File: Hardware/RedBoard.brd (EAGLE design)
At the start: 68.6 x 54.4 mm, 65 parts, among them IC3 LM1117, J1 POWER_JACKOVERPASTE_REDBOARD_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, J2 ICSP, Q1 ZXMP6A13FTA, Q2 2N7002PW, U1 FT231XS, U2 MIC5205, U3 ATMEGA328, Y1 16MHz

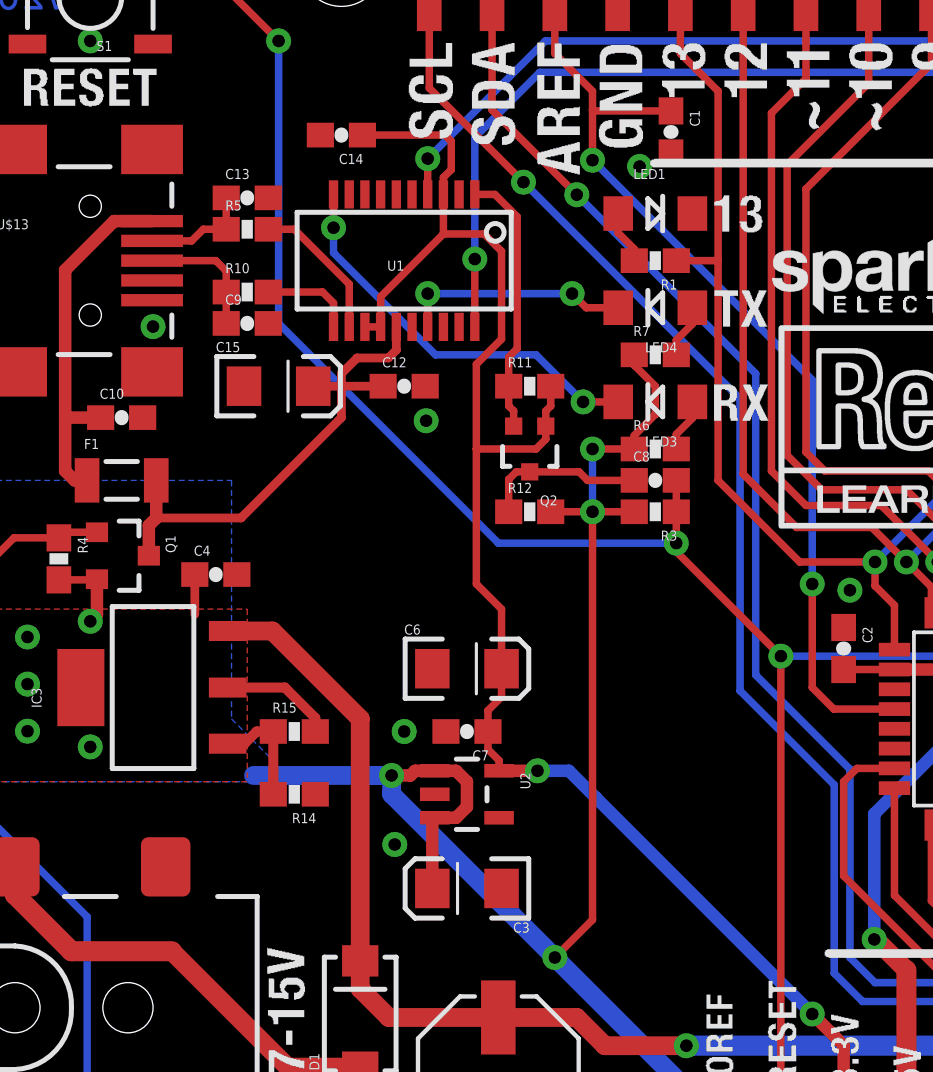
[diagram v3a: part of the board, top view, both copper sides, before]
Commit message: Spacing out caps and resistors
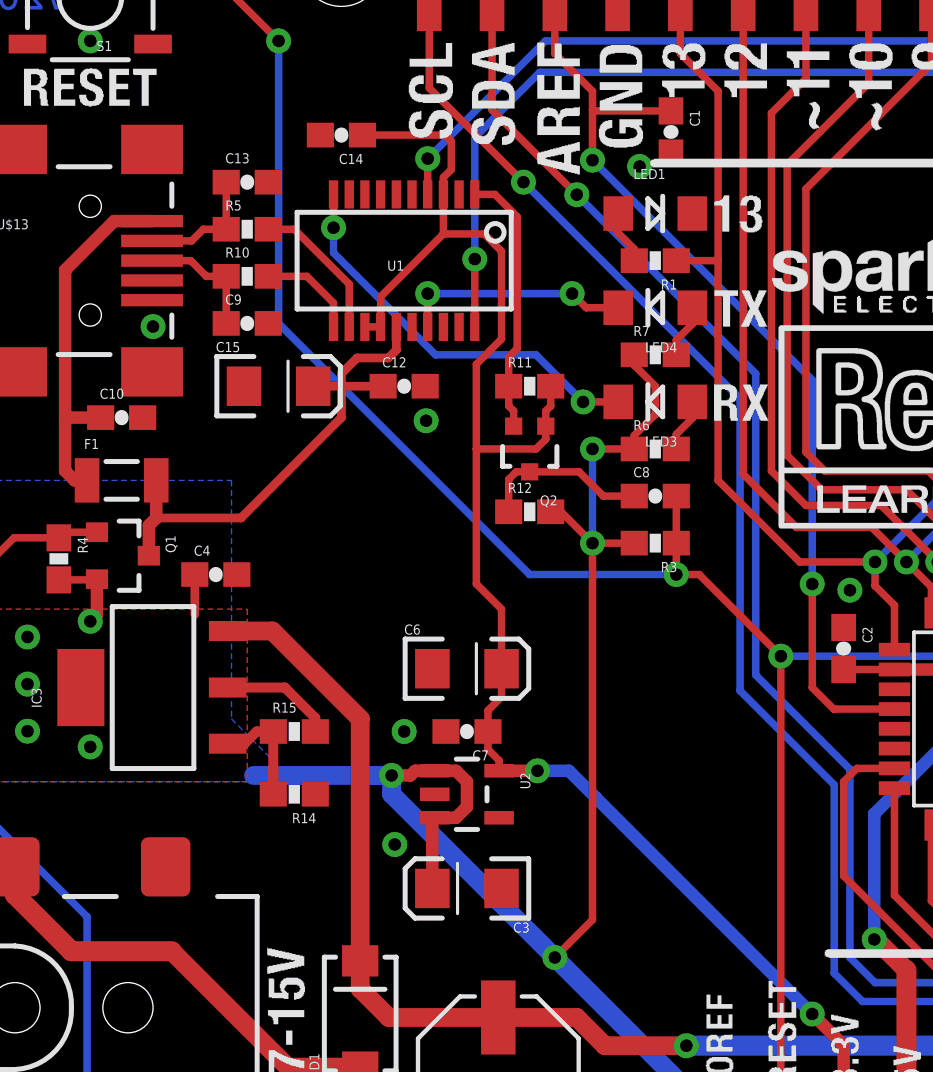
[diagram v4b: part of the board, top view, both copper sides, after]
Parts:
- moved R3 1.27 mm to (27.9, 27.9)
- moved C13 0.64 mm to (11.4, 42.5)
- moved C8 0.64 mm to (27.9, 29.8)
- moved R10 0.63 mm to (11.4, 38.7)
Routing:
- net D-: track 4.46 -> 5.10 mm
- net 5V: track 165.1 -> 165.7 mm
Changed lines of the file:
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@@
 <layer number="20" name="Dimension" color="15" fill="1" visible="yes" active="yes"/>
 <layer number="21" name="tPlace" color="16" fill="1" visible="yes" active="yes"/>
-<layer number="22" name="bPlace" color="14" fill="1" visible="no" active="yes"/>
+<layer number="22" name="bPlace" color="14" fill="1" visible="yes" active="yes"/>
 <layer number="23" name="tOrigins" color="15" fill="1" visible="yes" active="yes"/>
 <layer number="24" name="bOrigins" color="15" fill="1" visible="yes" active="yes"/>
@@
 <layer number="47" name="Measures" color="7" fill="1" visible="no" active="yes"/>
 <layer number="48" name="Document" color="7" fill="1" visible="no" active="yes"/>
-<layer number="49" name="ReferenceLC" color="13" fill="1" visible="yes" active="yes"/>
+<layer number="49" name="ReferenceLC" color="13" fill="1" visible="no" active="yes"/>
 <layer number="50" name="ReferenceLS" color="12" fill="1" visible="no" active="yes"/>
 <layer number="51" name="tDocu" color="6" fill="1" visible="yes" active="yes"/>
@@
 </element>
 <element name="R2" library="SparkFun" package="0603-RES" value="1k" x="58.42" y="34.29"/>
-<element name="R3" library="SparkFun" package="0603-RES" value="10k" x="27.94" y="29.21" smashed="yes" rot="R180">
-<attribute name="NAME" x="28.829" y="28.448" size="0.4064" layer="25" font="vector" rot="R180"/>
-<attribute name="VALUE" x="29.464" y="29.083" size="0.4064" layer="27" font="vector"/>
+<element name="R3" library="SparkFun" package="0603-RES" value="10k" x="27.94" y="27.94" smashed="yes" rot="R180">
+<attribute name="NAME" x="28.829" y="27.178" size="0.4064" layer="25" font="vector" rot="R180"/>
+<attribute name="VALUE" x="29.464" y="27.813" size="0.4064" layer="27" font="vector"/>
 </element>
 <element name="S1" library="SparkFun" package="TACTILE_SWITCH_SMD" value="RESET" x="5.08" y="50.038" rot="R180"/>
@@
 <attribute name="VALUE" x="4.826" y="28.829" size="0.4064" layer="27"/>
 </element>
-<element name="C8" library="SparkFun" package="0603-CAP" value="0.1uF" x="27.94" y="30.48" smashed="yes">
-<attribute name="NAME" x="27.051" y="31.242" size="0.4064" layer="25" font="vector"/>
-<attribute name="VALUE" x="29.464" y="30.226" size="0.4064" layer="27" font="vector"/>
+<element name="C8" library="SparkFun" package="0603-CAP" value="0.1uF" x="27.94" y="29.845" smashed="yes">
+<attribute name="NAME" x="27.051" y="30.607" size="0.4064" layer="25" font="vector"/>
+<attribute name="VALUE" x="29.464" y="29.591" size="0.4064" layer="27" font="vector"/>
 </element>
 <element name="C10" library="SparkFun" package="0603-CAP" value="0.1uF" x="6.35" y="33.02"/>
@@
 <attribute name="VALUE" x="11.176" y="39.624" size="0.4064" layer="27" font="vector"/>
 </element>
-<element name="R10" library="SparkFun-Resistors" package="0603-RES" value="27" x="11.43" y="38.1" smashed="yes">
-<attribute name="NAME" x="10.541" y="38.862" size="0.4064" layer="25" font="vector"/>
-<attribute name="VALUE" x="11.176" y="38.735" size="0.4064" layer="27" font="vector"/>
+<element name="R10" library="SparkFun-Resistors" package="0603-RES" value="27" x="11.43" y="38.735" smashed="yes">
+<attribute name="NAME" x="10.541" y="39.497" size="0.4064" layer="25" font="vector"/>
+<attribute name="VALUE" x="11.176" y="39.37" size="0.4064" layer="27" font="vector"/>
 </element>
 <element name="C9" library="SparkFun-Capacitors" package="0603-CAP" value="47pF" x="11.43" y="36.83" smashed="yes">
@@
 <attribute name="VALUE" x="10.795" y="35.814" size="0.4064" layer="27" font="vector"/>
 </element>
-<element name="C13" library="SparkFun-Capacitors" package="0603-CAP" value="47pF" x="11.43" y="41.91" smashed="yes">
-<attribute name="PROD_ID" value="CAP-08913" x="11.43" y="41.91" size="1.016" layer="27" font="vector" ratio="15" display="off"/>
-<attribute name="NAME" x="10.541" y="42.672" size="0.4064" layer="25" font="vector"/>
-<attribute name="VALUE" x="10.922" y="42.545" size="0.4064" layer="27" font="vector"/>
+<element name="C13" library="SparkFun-Capacitors" package="0603-CAP" value="47pF" x="11.43" y="42.545" smashed="yes">
+<attribute name="PROD_ID" value="CAP-08913" x="11.43" y="42.545" size="1.016" layer="27" font="vector" ratio="15" display="off"/>
+<attribute name="NAME" x="10.541" y="43.307" size="0.4064" layer="25" font="vector"/>
+<attribute name="VALUE" x="10.922" y="43.18" size="0.4064" layer="27" font="vector"/>
 </element>
 <element name="C14" library="SparkFun" package="0603-CAP" value="0.1uF" x="15.24" y="44.45" rot="R180"/>
@@
 <contactref element="R12" pad="2"/>
 <via x="25.4" y="31.75" extent="1-16" drill="0.508"/>
-<via x="25.4" y="29.21" extent="1-16" drill="0.508"/>
+<via x="25.4" y="27.94" extent="1-16" drill="0.508"/>
 <via x="23.876" y="11.176" extent="1-16" drill="0.508"/>
 <via x="47.771" y="20.428" extent="1-16" drill="0.508"/>
@@
 <wire x1="67.31" y1="30.988" x2="66.04" y2="30.988" width="0.254" layer="1"/>
 <wire x1="66.04" y1="32.258" x2="66.04" y2="30.988" width="0.3048" layer="1"/>
-<wire x1="23.71" y1="29.21" x2="25.4" y2="29.21" width="0.3048" layer="1"/>
-<wire x1="25.4" y1="29.21" x2="25.4" y2="12.7" width="0.3048" layer="1"/>
+<wire x1="25.4" y1="27.94" x2="25.4" y2="12.7" width="0.3048" layer="1"/>
 <wire x1="25.4" y1="12.7" x2="23.876" y2="11.176" width="0.3048" layer="1"/>
-<wire x1="25.4" y1="29.21" x2="25.4" y2="31.75" width="0.3048" layer="16"/>
+<wire x1="25.4" y1="27.94" x2="25.4" y2="31.75" width="0.3048" layer="16"/>
 <wire x1="27.09" y1="31.75" x2="25.4" y2="31.75" width="0.3048" layer="1"/>
-<wire x1="25.4" y1="29.21" x2="27.09" y2="29.21" width="0.3048" layer="1"/>
+<wire x1="25.4" y1="27.94" x2="27.09" y2="27.94" width="0.3048" layer="1"/>
 <wire x1="27.09" y1="35.56" x2="27.09" y2="35.14" width="0.3048" layer="1"/>
 <wire x1="27.09" y1="35.14" x2="27.94" y2="34.29" width="0.3048" layer="1"/>
@@
 <wire x1="23.876" y1="11.176" x2="17.272" y2="17.78" width="0.762" layer="16"/>
 <wire x1="17.272" y1="17.78" x2="17.272" y2="18.542" width="0.762" layer="16"/>
+<wire x1="23.71" y1="29.21" x2="24.13" y2="29.21" width="0.3048" layer="1"/>
+<wire x1="24.13" y1="29.21" x2="25.4" y2="27.94" width="0.3048" layer="1"/>
 </signal>
 <signal name="GND">
@@
 <wire x1="62.992" y1="25.908" x2="63.5" y2="25.4" width="0.3048" layer="1"/>
 <wire x1="12.7" y1="48.26" x2="12.7" y2="36.83" width="0.3048" layer="16"/>
-<wire x1="12.7" y1="36.83" x2="21.59" y2="27.94" width="0.3048" layer="16"/>
-<wire x1="21.59" y1="27.94" x2="28.79" y2="27.94" width="0.3048" layer="16"/>
-<via x="28.79" y="27.94" extent="1-16" drill="0.508"/>
-<wire x1="28.79" y1="27.94" x2="28.79" y2="29.21" width="0.3048" layer="1"/>
-<wire x1="28.79" y1="29.21" x2="28.79" y2="30.48" width="0.3048" layer="1"/>
+<wire x1="12.7" y1="36.83" x2="22.86" y2="26.67" width="0.3048" layer="16"/>
+<wire x1="28.79" y1="27.94" x2="28.79" y2="29.845" width="0.3048" layer="1"/>
 <contactref element="TP6" pad="P$1"/>
 <via x="63.5" y="25.908" extent="1-16" drill="0.508"/>
 <wire x1="62.992" y1="25.908" x2="63.5" y2="25.908" width="0.3048" layer="1"/>
-<wire x1="33.02" y1="23.368" x2="28.79" y2="27.598" width="0.3048" layer="1"/>
-<wire x1="28.79" y1="27.598" x2="28.79" y2="27.94" width="0.3048" layer="1"/>
+<wire x1="22.86" y1="26.67" x2="28.79" y2="26.67" width="0.3048" layer="16"/>
+<via x="28.79" y="26.67" extent="1-16" drill="0.508"/>
+<wire x1="33.02" y1="23.368" x2="29.718" y2="26.67" width="0.3048" layer="1"/>
+<wire x1="29.718" y1="26.67" x2="28.79" y2="26.67" width="0.3048" layer="1"/>
+<wire x1="28.79" y1="27.94" x2="28.79" y2="26.67" width="0.3048" layer="1"/>
 </signal>
 <signal name="AREF">
@@
 <wire x1="22.86" y1="30.825" x2="22.316" y2="30.825" width="0.3048" layer="1"/>
 <wire x1="22.86" y1="30.825" x2="24.856" y2="30.825" width="0.3048" layer="1"/>
-<wire x1="27.09" y1="30.48" x2="25.201" y2="30.48" width="0.3048" layer="1"/>
-<wire x1="25.201" y1="30.48" x2="24.856" y2="30.825" width="0.3048" layer="1"/>
+<wire x1="27.09" y1="29.845" x2="25.836" y2="29.845" width="0.3048" layer="1"/>
+<wire x1="25.836" y1="29.845" x2="24.856" y2="30.825" width="0.3048" layer="1"/>
 </signal>
 <signal name="D-">
@@
 <wire x1="9.182" y1="40.17" x2="9.652" y2="40.64" width="0.3048" layer="1"/>
 <wire x1="10.58" y1="40.64" x2="9.652" y2="40.64" width="0.3048" layer="1"/>
-<wire x1="10.58" y1="40.64" x2="10.58" y2="41.91" width="0.3048" layer="1"/>
+<wire x1="10.58" y1="40.64" x2="10.58" y2="42.545" width="0.3048" layer="1"/>
 </signal>
 <signal name="D+">
@@
 <contactref element="R10" pad="1"/>
 <contactref element="C9" pad="1"/>
-<wire x1="7.58" y1="39.37" x2="10.16" y2="39.37" width="0.3048" layer="1"/>
-<wire x1="10.16" y1="39.37" x2="10.58" y2="38.95" width="0.3048" layer="1"/>
-<wire x1="10.58" y1="38.1" x2="10.58" y2="38.95" width="0.3048" layer="1"/>
-<wire x1="10.58" y1="36.83" x2="10.58" y2="38.1" width="0.3048" layer="1"/>
+<wire x1="10.58" y1="38.735" x2="10.58" y2="38.95" width="0.3048" layer="1"/>
+<wire x1="7.58" y1="39.37" x2="9.144" y2="39.37" width="0.3048" layer="1"/>
+<wire x1="9.144" y1="39.37" x2="9.779" y2="38.735" width="0.3048" layer="1"/>
+<wire x1="10.58" y1="38.735" x2="9.779" y2="38.735" width="0.3048" layer="1"/>
+<wire x1="10.58" y1="36.83" x2="10.58" y2="38.735" width="0.3048" layer="1"/>
 </signal>
 <signal name="VUSB">
@@
 <contactref element="U1" pad="11"/>
 <contactref element="R10" pad="2"/>
-<wire x1="12.28" y1="38.1" x2="14.478" y2="38.1" width="0.3048" layer="1"/>
 <wire x1="14.9225" y1="36.6903" x2="14.9225" y2="37.6555" width="0.3048" layer="1"/>
-<wire x1="14.9225" y1="37.6555" x2="14.478" y2="38.1" width="0.3048" layer="1"/>
+<wire x1="12.28" y1="38.735" x2="13.843" y2="38.735" width="0.3048" layer="1"/>
+<wire x1="13.843" y1="38.735" x2="14.9225" y2="37.6555" width="0.3048" layer="1"/>
 </signal>
 <signal name="N$12">

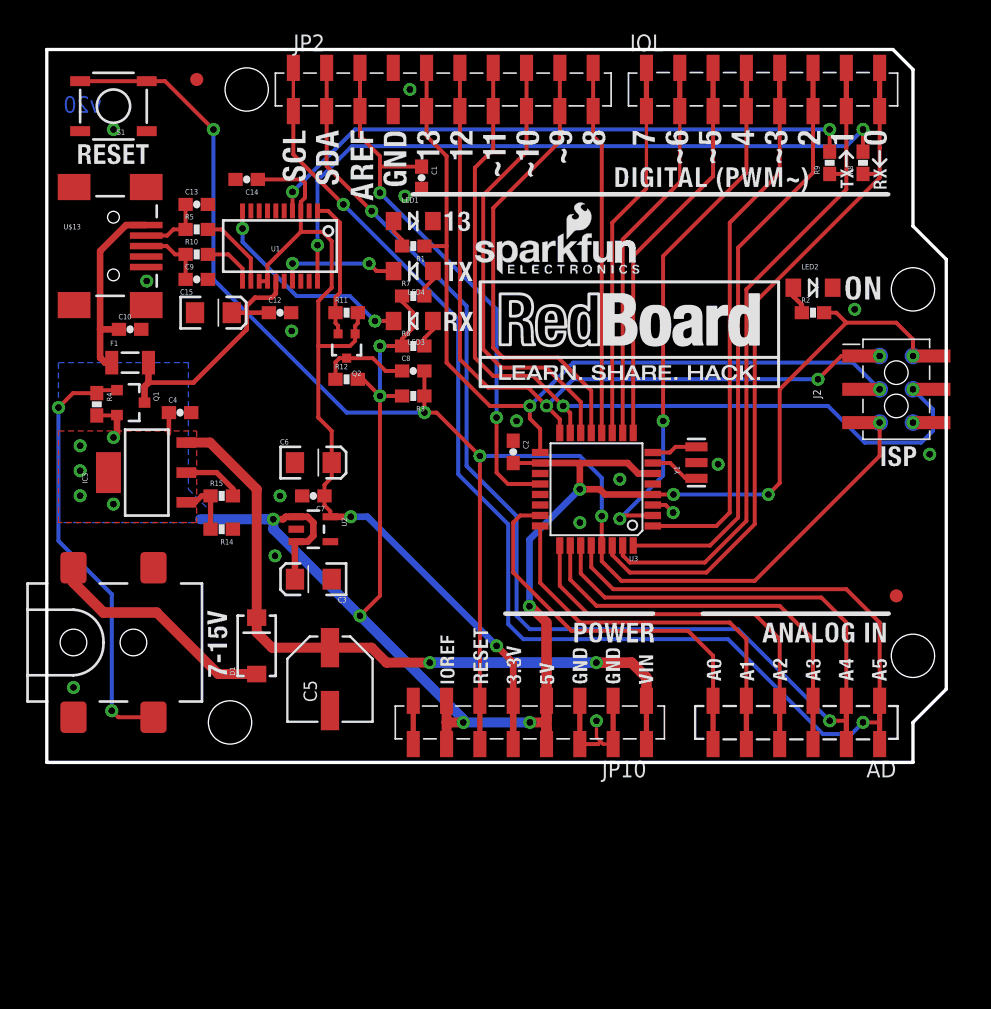
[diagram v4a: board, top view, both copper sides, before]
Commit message: Moved C1 cap around silk. Moved some top silk.
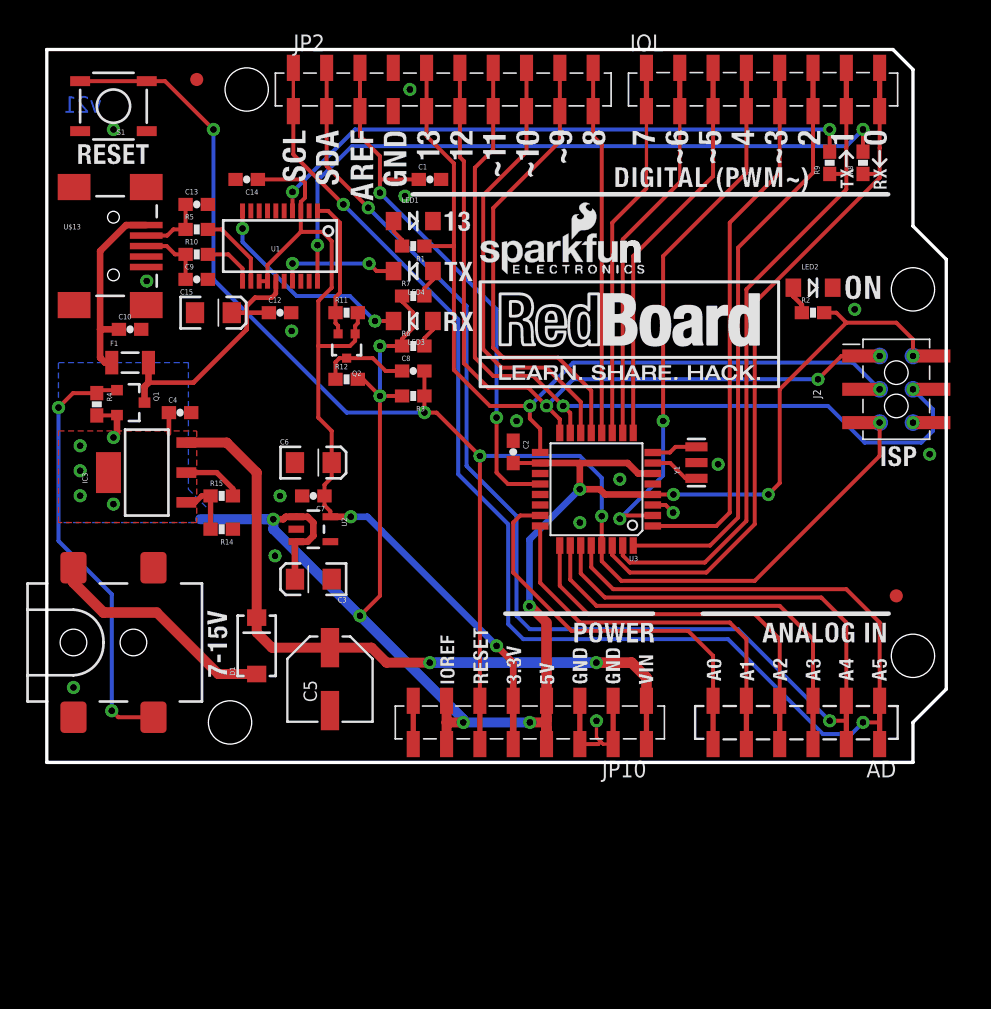
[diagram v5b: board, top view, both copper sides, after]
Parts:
- moved C1 0.65 mm to (29.2, 44.5), turned to 0 degrees
- moved JP1 0.38 mm to (33.0, 37.2)
- moved JP7 0.38 mm to (40.0, 39.9)
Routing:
- net VIN: track 54.0 -> 54.7 mm
- net SCK: track 66.5 -> 67.1 mm
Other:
- board text added: "v21"
- board text removed: "v20"
